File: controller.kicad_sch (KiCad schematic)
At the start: 40 parts, among them J201 SWD, J202 USB_C_Receptacle_USB2.0_16P, SW201 CL-SB_22A-12T, U201 ULN2803A, U202 IP4234CZ6, U203 STM32G431CBTx, U204 MCP2542FDxMF, U205 ILD74, Y201 24MHz

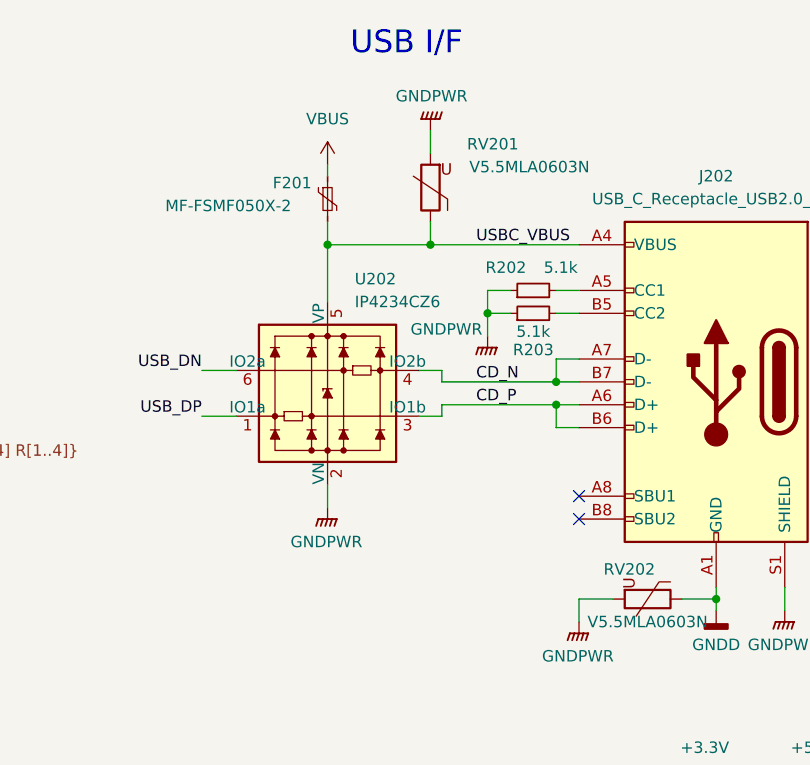
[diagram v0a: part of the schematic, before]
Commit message: Many more vias, improved some routing
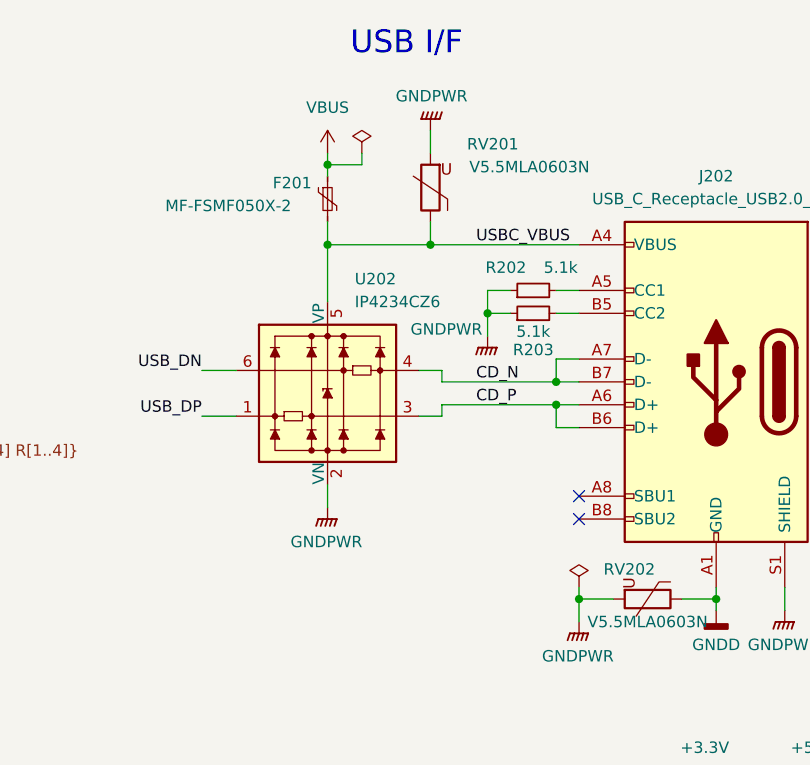
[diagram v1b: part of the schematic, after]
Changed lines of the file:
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@@
 	)
 	(junction
+		(at 247.65 78.74)
+		(diameter 0)
+		(color 0 0 0 0)
+	)
+	(junction
+		(at 219.71 30.48)
+		(diameter 0)
+		(color 0 0 0 0)
+	)
+	(junction
 		(at 255.27 147.32)
 		(diameter 0)
@@
 	(wire
 		(pts
+			(xy 219.71 30.48) (xy 219.71 31.75)
+		)
+		(stroke
+			(width 0)
+			(type default)
+		)
+	)
+	(wire
+		(pts
 			(xy 153.67 46.99) (xy 165.1 46.99)
 		)
@@
 	(wire
 		(pts
+			(xy 247.65 77.47) (xy 247.65 78.74)
+		)
+		(stroke
+			(width 0)
+			(type default)
+		)
+	)
+	(wire
+		(pts
 			(xy 99.06 26.67) (xy 96.52 26.67)
 		)
@@
 	(wire
 		(pts
-			(xy 219.71 30.48) (xy 219.71 31.75)
+			(xy 219.71 29.21) (xy 219.71 30.48)
 		)
 		(stroke
@@
 	(wire
 		(pts
+			(xy 223.52 30.48) (xy 219.71 30.48)
+		)
+		(stroke
+			(width 0)
+			(type default)
+		)
+	)
+	(wire
+		(pts
 			(xy 212.09 153.67) (xy 212.09 154.94)
 		)
@@
 	(wire
 		(pts
+			(xy 223.52 29.21) (xy 223.52 30.48)
+		)
+		(stroke
+			(width 0)
+			(type default)
+		)
+	)
+	(wire
+		(pts
 			(xy 33.02 149.86) (xy 35.56 149.86)
 		)
@@
 	(symbol
 		(lib_id "power:VBUS")
-		(at 219.71 30.48 0)
+		(at 219.71 29.21 0)
 		(unit 1)
 		(exclude_from_sim no)
@@
 		(fields_autoplaced yes)
 		(property "Reference" "#PWR0205"
-			(at 219.71 34.29 0)
+			(at 219.71 33.02 0)
 			(effects
 				(font
@@
 		)
 		(property "Value" "VBUS"
-			(at 219.71 25.4 0)
+			(at 219.71 24.13 0)
 			(effects
 				(font
@@
 		)
 		(property "Footprint" ""
-			(at 219.71 30.48 0)
+			(at 219.71 29.21 0)
 			(effects
 				(font
@@
 		)
 		(property "Datasheet" ""
-			(at 219.71 30.48 0)
+			(at 219.71 29.21 0)
 			(effects
 				(font
@@
 		)
 		(property "Description" "Power symbol creates a global label with name \"VBUS\""
-			(at 219.71 30.48 0)
+			(at 219.71 29.21 0)
 			(effects
 				(font
@@
 	)
 	(symbol
+		(lib_id "power:PWR_FLAG")
+		(at 223.52 29.21 0)
+		(unit 1)
+		(exclude_from_sim no)
+		(in_bom yes)
+		(on_board yes)
+		(dnp no)
+		(fields_autoplaced yes)
+		(property "Reference" "#FLG0201"
+			(at 223.52 27.305 0)
+			(effects
+				(font
+					(size 1.27 1.27)
+				)
+				(hide yes)
+			)
+		)
+		(property "Value" "PWR_FLAG"
+			(at 223.52 24.13 0)
+			(effects
+				(font
+					(size 1.27 1.27)
+				)
+				(hide yes)
+			)
+		)
+		(property "Footprint" ""
+			(at 223.52 29.21 0)
+			(effects
+				(font
+					(size 1.27 1.27)
+				)
+				(hide yes)
+			)
+		)
+		(property "Datasheet" "~"
+			(at 223.52 29.21 0)
+			(effects
+				(font
+					(size 1.27 1.27)
+				)
+				(hide yes)
+			)
+		)
+		(property "Description" "Special symbol for telling ERC where power comes from"
+			(at 223.52 29.21 0)
+			(effects
+				(font
+					(size 1.27 1.27)
+				)
+				(hide yes)
+			)
+		)
+		(pin "1"
+		)
+		(instances
+			(project "ZFTuner"
+				(path "/fdb95973-bff7-44bf-8fa0-11fcc1e3382d/6bf6105b-2249-4510-b91e-560ebaed8aef"
+					(reference "#FLG0201")
+					(unit 1)
+				)
+			)
+		)
+	)
+	(symbol
 		(lib_id "Device:R_Small")
 		(at 142.24 105.41 0)
@@
 			)
 		)
-		(property "Description" "ESD Protection USB 2.0 to IEC 61000-4-2 level 4, 5.5V, SOT457 (SC-74-6)"
+		(property "Description" "ESD Protection, 2 channel, USB 2.0 to IEC 61000-4-2 level 4, 5.5V, SOT457 (SC-74-6)"
 			(at 219.71 73.914 0)
 			(effects
@@
 					(unit 1)
 				)
+			)
+		)
+	)
+	(symbol
+		(lib_id "power:PWR_FLAG")
+		(at 247.65 77.47 0)
+		(unit 1)
+		(exclude_from_sim no)
+		(in_bom yes)
+		(on_board yes)
+		(dnp no)
+		(fields_autoplaced yes)
+		(property "Reference" "#FLG0202"
+			(at 247.65 75.565 0)
+			(effects
+				(font
+					(size 1.27 1.27)
+				)
+				(hide yes)
+			)
+		)
+		(property "Value" "PWR_FLAG"
+			(at 247.65 72.39 0)
+			(effects
+				(font
+					(size 1.27 1.27)
+				)
+				(hide yes)
+			)
+		)
+		(property "Footprint" ""
+			(at 247.65 77.47 0)
+			(effects
+				(font
+					(size 1.27 1.27)
+				)
+				(hide yes)
+			)
+		)
+		(property "Datasheet" "~"
+			(at 247.65 77.47 0)
+			(effects
+				(font
+					(size 1.27 1.27)
+				)
+				(hide yes)
+			)
+		)
+		(property "Description" "Special symbol for telling ERC where power comes from"
+			(at 247.65 77.47 0)
+			(effects
+				(font
+					(size 1.27 1.27)
+				)
+				(hide yes)
+			)
+		)
+		(pin "1"
+		)
+		(instances
+			(project "ZFTuner"
+				(path "/fdb95973-bff7-44bf-8fa0-11fcc1e3382d/6bf6105b-2249-4510-b91e-560ebaed8aef"
+					(reference "#FLG0202")
+					(unit 1)
+				)

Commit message: Some schematic cleanup and minor fixes
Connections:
- net Relays.R1 is gone; now on net R1: U201.17 (O2)
- net Relays.R2 is gone; now on net R2: U201.15 (O4)
- net Relays.R3 is gone; now on net R3: U201.13 (O6)
- net Relays.R4 is gone; now on net R4: U201.11 (O8)
- net Relays.S1 is gone; now on net S1: U201.18 (O1)
- net Relays.S2 is gone; now on net S2: U201.16 (O3)
- net Relays.S3 is gone; now on net S3: U201.14 (O5)
- net Relays.S4 is gone; now on net S4: U201.12 (O7)
- net R1: no longer U201.2 (I2), U203.30 (PA8)
- net R2: no longer U201.4 (I4), U203.14 (PA6)
- net R3: no longer U201.6 (I6), U203.12 (PA4)
- net R4: no longer U201.8 (I8), U203.10 (PA2)
- net S1: no longer U201.1 (I1), U203.31 (PA9)
- net S2: no longer U201.3 (I3), U203.15 (PA7)
- net S3: no longer U201.5 (I5), U203.13 (PA5)
- net S4: no longer U201.7 (I7), U203.11 (PA3)
- new net C_R1: U201.2 (I2), U203.30 (PA8)
- new net C_R2: U201.4 (I4), U203.14 (PA6)
- new net C_R3: U201.6 (I6), U203.12 (PA4)
- new net C_R4: U201.8 (I8), U203.10 (PA2)
- new net C_S1: U201.1 (I1), U203.31 (PA9)
- new net C_S2: U201.3 (I3), U203.15 (PA7)
- new net C_S3: U201.5 (I5), U203.13 (PA5)
- new net C_S4: U201.7 (I7), U203.11 (PA3)

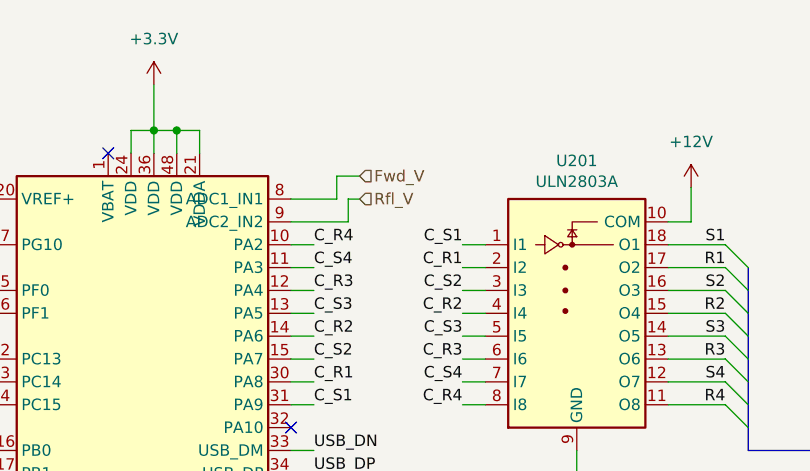
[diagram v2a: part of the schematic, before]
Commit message: Improved grounding
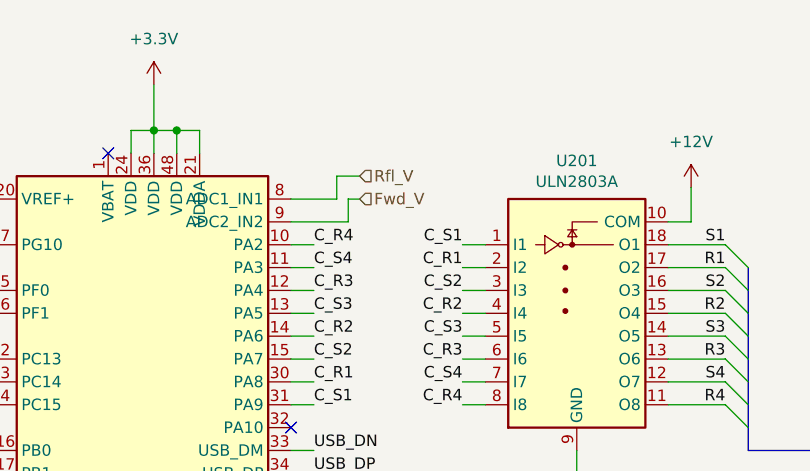
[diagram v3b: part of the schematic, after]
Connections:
- net Fwd_V: now also U203.9 (PA1); no longer U203.8 (PA0)
- net Rfl_V: now also U203.8 (PA0); no longer U203.9 (PA1)
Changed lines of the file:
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@@
 	(hierarchical_label "Fwd_V"
 		(shape input)
-		(at 119.38 31.75 0)
+		(at 119.38 34.29 0)
 		(fields_autoplaced yes)
 		(effects
@@
 	(hierarchical_label "Rfl_V"
 		(shape input)
-		(at 119.38 34.29 0)
+		(at 119.38 31.75 0)
 		(fields_autoplaced yes)
 		(effects
